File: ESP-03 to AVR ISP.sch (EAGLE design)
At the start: 17 parts, among them J1 AVR_SPI_PRG_62X3_LOCK, Q1 MOSFET-NCHANNELBSS138

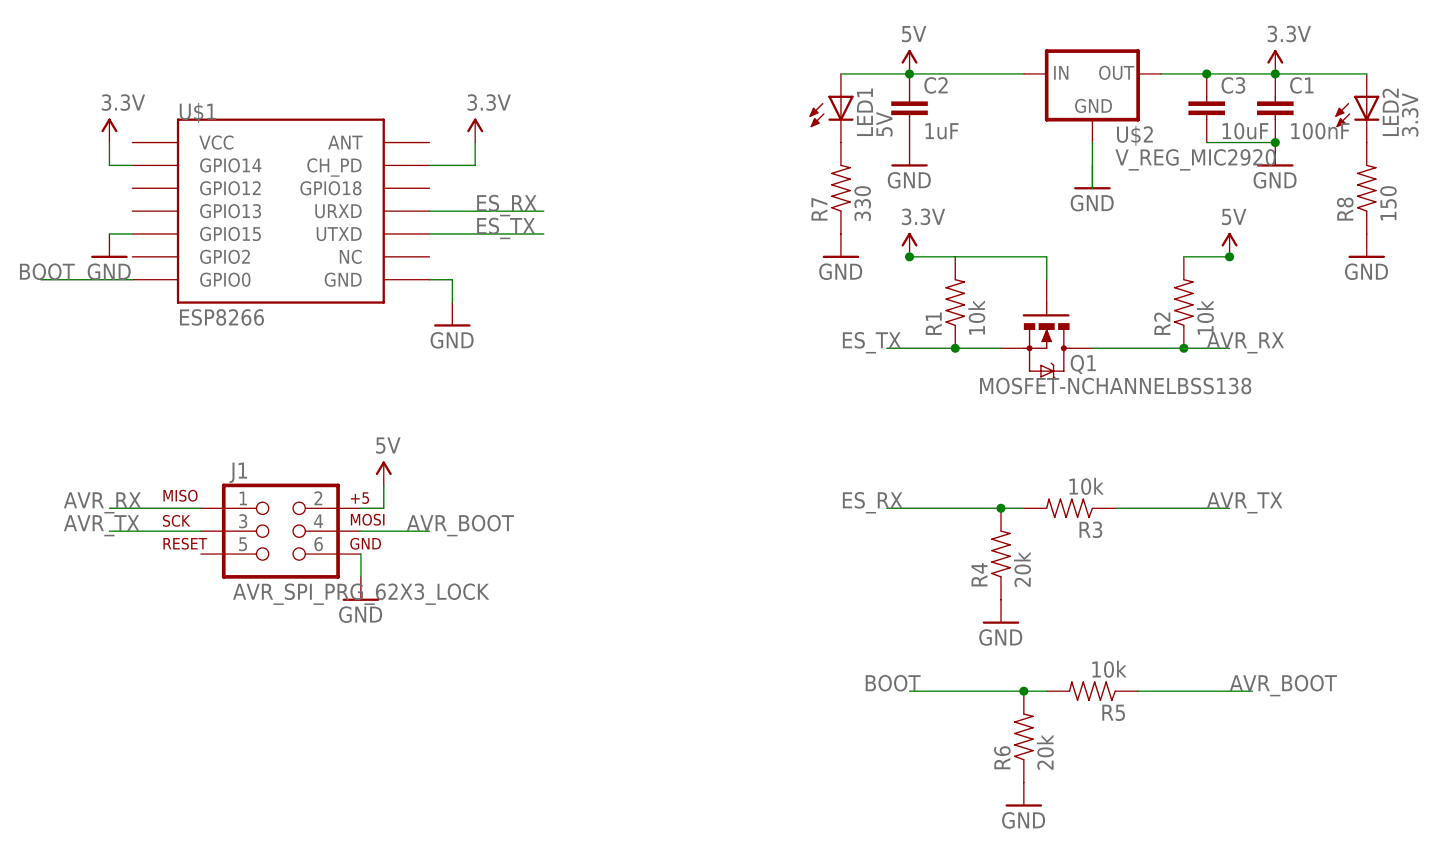
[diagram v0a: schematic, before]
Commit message: PCB: Fixed wrong VCC connection. Removed Bootloader voltage divider. Changed LDO to 1117type
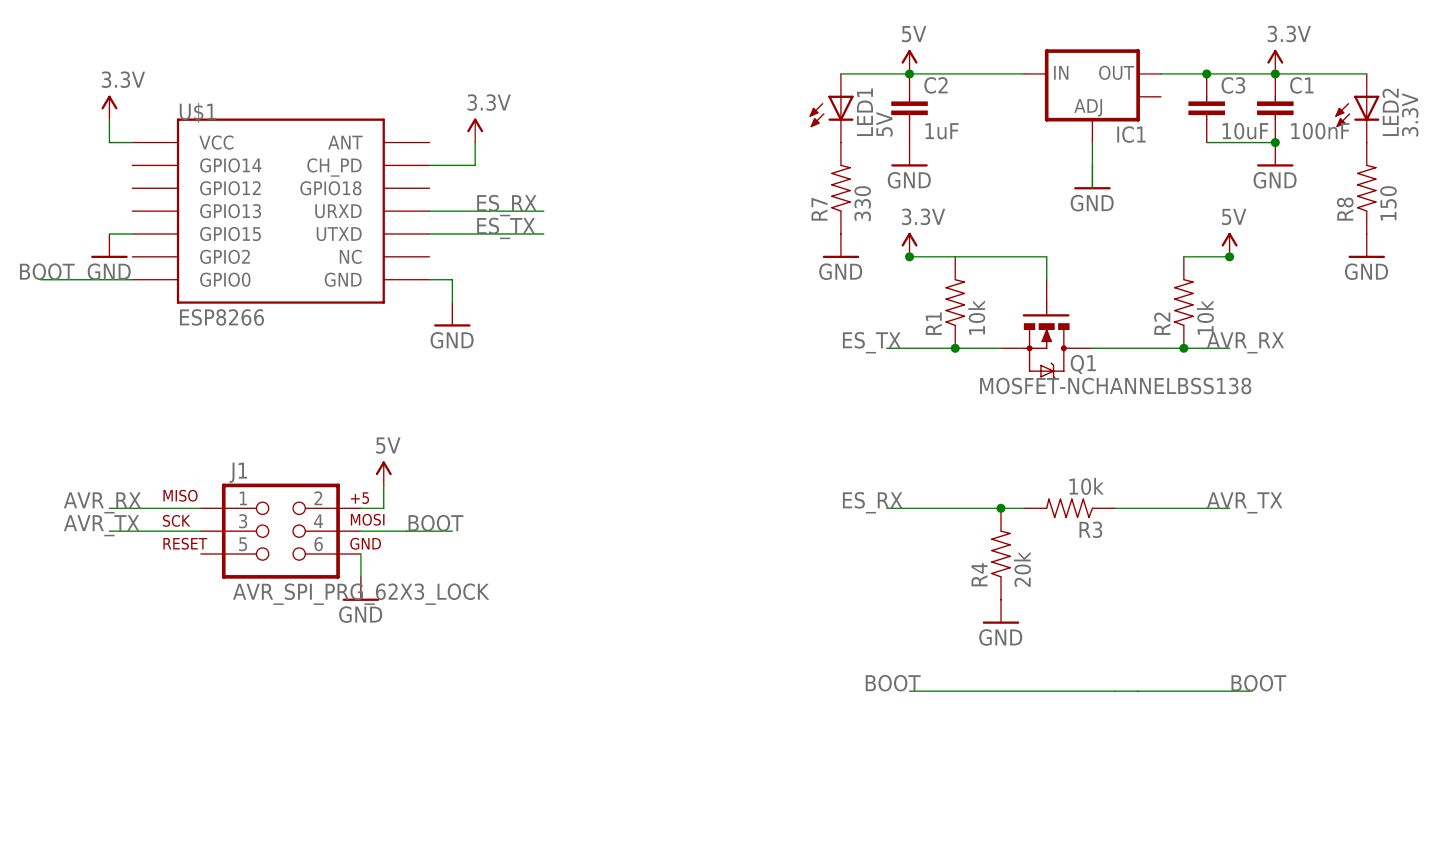
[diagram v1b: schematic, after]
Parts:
- removed R5: 10k, SparkFun-Resistors:RESISTOR0603-RES
- removed R6: 20k, SparkFun-Resistors:RESISTOR0603-RES
- removed U$2: V_REG_MIC2920, SparkFun-PowerIC:V_REG_MIC2920
- added IC1: (no value), SparkFun-PowerIC:V_REG_LM1117SOT223
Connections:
- removed net AVR_BOOT: J1.4, R5.1
- net 3.3V: now also IC1.OUT, U$1.VCC; no longer U$1.GPIO14, U$2.OUT
- net 5V: now also IC1.IN; no longer U$2.IN
- net BOOT: now also J1.4; no longer R5.2, R6.2
- net GND: now also IC1.ADJ; no longer R6.1, U$2.GND
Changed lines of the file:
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@@
 <part name="GND3" library="supply1" deviceset="GND" device=""/>
 <part name="U$1" library="esp8266modules" deviceset="ESP8266" device=""/>
-<part name="U$2" library="SparkFun-PowerIC" deviceset="V_REG_MIC2920" device=""/>
 <part name="J1" library="SparkFun-Connectors" deviceset="AVR_SPI_PRG_6" device="2X3_LOCK"/>
 <part name="SUPPLY1" library="SparkFun-Aesthetics" deviceset="3.3V" device=""/>
@@
 <part name="SUPPLY7" library="SparkFun-Aesthetics" deviceset="5V" device=""/>
 <part name="GND7" library="supply1" deviceset="GND" device=""/>
-<part name="R5" library="SparkFun-Resistors" deviceset="RESISTOR" device="0603-RES" value="10k"/>
-<part name="R6" library="SparkFun-Resistors" deviceset="RESISTOR" device="0603-RES" value="20k"/>
-<part name="GND8" library="supply1" deviceset="GND" device=""/>
 <part name="LED1" library="SparkFun-LED" deviceset="LED" device="0603" value="5V"/>
 <part name="LED2" library="SparkFun-LED" deviceset="LED" device="0603" value="3.3V"/>
@@
 <part name="GND9" library="supply1" deviceset="GND" device=""/>
 <part name="GND10" library="supply1" deviceset="GND" device=""/>
+<part name="IC1" library="SparkFun-PowerIC" deviceset="V_REG_LM1117" device="SOT223"/>
 </parts>
 <sheets>
@@
 <instance part="GND3" gate="1" x="15.24" y="63.5"/>
 <instance part="U$1" gate="G$1" x="-53.34" y="58.42"/>
-<instance part="U$2" gate="G$1" x="35.56" y="73.66"/>
 <instance part="J1" gate="G$1" x="-55.88" y="22.86"/>
 <instance part="SUPPLY1" gate="G$1" x="55.88" y="73.66"/>
@@
 <instance part="GND4" gate="1" x="25.4" y="12.7"/>
 <instance part="SUPPLY3" gate="G$1" x="-33.02" y="66.04"/>
-<instance part="SUPPLY6" gate="G$1" x="-73.66" y="66.04"/>
+<instance part="SUPPLY6" gate="G$1" x="-73.66" y="68.58"/>
 <instance part="GND5" gate="1" x="-35.56" y="45.72"/>
 <instance part="GND6" gate="1" x="-73.66" y="53.34"/>
 <instance part="SUPPLY7" gate="G$1" x="-43.18" y="27.94"/>
 <instance part="GND7" gate="1" x="-45.72" y="15.24"/>
-<instance part="R5" gate="G$1" x="35.56" y="5.08" rot="R180"/>
-<instance part="R6" gate="G$1" x="27.94" y="0" rot="R90"/>
-<instance part="GND8" gate="1" x="27.94" y="-7.62"/>
 <instance part="LED1" gate="G$1" x="7.62" y="71.12"/>
 <instance part="LED2" gate="G$1" x="66.04" y="71.12"/>
@@
 <instance part="GND9" gate="1" x="7.62" y="53.34"/>
 <instance part="GND10" gate="1" x="66.04" y="53.34"/>
+<instance part="IC1" gate="G$1" x="35.56" y="73.66"/>
 </instances>
 <busses>
@@
 <pinref part="GND1" gate="1" pin="GND"/>
 <wire x1="35.56" y1="63.5" x2="35.56" y2="60.96" width="0.1524" layer="91"/>
-<pinref part="U$2" gate="G$1" pin="GND"/>
 <wire x1="35.56" y1="66.04" x2="35.56" y2="63.5" width="0.1524" layer="91"/>
+<pinref part="IC1" gate="G$1" pin="ADJ"/>
 </segment>
 <segment>
@@
 <pinref part="J1" gate="G$1" pin="6"/>
 <wire x1="-45.72" y1="17.78" x2="-45.72" y2="20.32" width="0.1524" layer="91"/>
-</segment>
-<segment>
-<pinref part="R6" gate="G$1" pin="1"/>
-<pinref part="GND8" gate="1" pin="GND"/>
 </segment>
 <segment>
@@
 <wire x1="55.88" y1="73.66" x2="48.26" y2="73.66" width="0.1524" layer="91"/>
 <junction x="55.88" y="73.66"/>
-<pinref part="U$2" gate="G$1" pin="OUT"/>
 <pinref part="SUPPLY1" gate="G$1" pin="3.3V"/>
 <pinref part="C3" gate="G$1" pin="1"/>
@@
 <pinref part="LED2" gate="G$1" pin="A"/>
 <wire x1="55.88" y1="73.66" x2="66.04" y2="73.66" width="0.1524" layer="91"/>
+<pinref part="IC1" gate="G$1" pin="OUT"/>
 </segment>
 <segment>
@@
 </segment>
 <segment>
-<pinref part="U$1" gate="G$1" pin="GPIO14"/>
 <pinref part="SUPPLY6" gate="G$1" pin="3.3V"/>
-<wire x1="-71.12" y1="63.5" x2="-73.66" y2="63.5" width="0.1524" layer="91"/>
-<wire x1="-73.66" y1="63.5" x2="-73.66" y2="66.04" width="0.1524" layer="91"/>
+<wire x1="-73.66" y1="66.04" x2="-73.66" y2="68.58" width="0.1524" layer="91"/>
+<pinref part="U$1" gate="G$1" pin="VCC"/>
+<wire x1="-73.66" y1="66.04" x2="-71.12" y2="66.04" width="0.1524" layer="91"/>
 </segment>
 </net>
@@
 <wire x1="15.24" y1="73.66" x2="27.94" y2="73.66" width="0.1524" layer="91"/>
 <junction x="15.24" y="73.66"/>
-<pinref part="U$2" gate="G$1" pin="IN"/>
 <pinref part="SUPPLY4" gate="G$1" pin="5V"/>
 <pinref part="LED1" gate="G$1" pin="A"/>
 <wire x1="7.62" y1="73.66" x2="15.24" y2="73.66" width="0.1524" layer="91"/>
+<pinref part="IC1" gate="G$1" pin="IN"/>
 </segment>
 <segment>
@@
 </segment>
 <segment>
-<pinref part="R5" gate="G$1" pin="2"/>
-<pinref part="R6" gate="G$1" pin="2"/>
-<wire x1="30.48" y1="5.08" x2="27.94" y2="5.08" width="0.1524" layer="91"/>
-<wire x1="27.94" y1="5.08" x2="15.24" y2="5.08" width="0.1524" layer="91"/>
+<wire x1="53.34" y1="5.08" x2="40.64" y2="5.08" width="0.1524" layer="91"/>
 <label x="10.16" y="5.08" size="1.778" layer="95"/>
-<junction x="27.94" y="5.08"/>
-</segment>
-</net>
-<net name="AVR_BOOT" class="0">
-<segment>
-<pinref part="R5" gate="G$1" pin="1"/>
-<wire x1="40.64" y1="5.08" x2="53.34" y2="5.08" width="0.1524" layer="91"/>
 <label x="50.8" y="5.08" size="1.778" layer="95"/>
+<wire x1="38.1" y1="5.08" x2="15.24" y2="5.08" width="0.1524" layer="91"/>
+<wire x1="40.64" y1="5.08" x2="38.1" y2="5.08" width="0.1524" layer="91"/>
 </segment>
 <segment>
 <pinref part="J1" gate="G$1" pin="4"/>
-<wire x1="-45.72" y1="22.86" x2="-38.1" y2="22.86" width="0.1524" layer="91"/>
+<wire x1="-45.72" y1="22.86" x2="-40.64" y2="22.86" width="0.1524" layer="91"/>
 <label x="-40.64" y="22.86" size="1.778" layer="95"/>
-</segment>
-</net>
+<wire x1="-40.64" y1="22.86" x2="-38.1" y2="22.86" width="0.1524" layer="91"/>
+<wire x1="-35.56" y1="22.86" x2="-38.1" y2="22.86" width="0.1524" layer="91"/>
+</segment>
+</net>

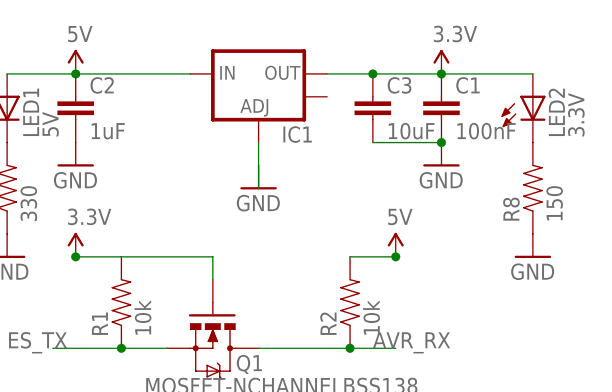
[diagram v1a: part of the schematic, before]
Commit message: Fixed PCB. Swithed to 1117 LDO.
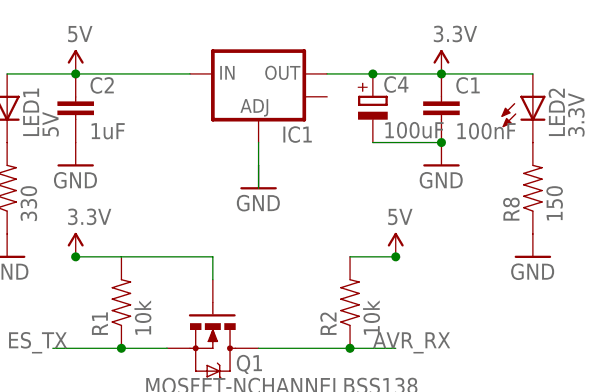
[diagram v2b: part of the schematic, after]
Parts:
- removed C3: 10uF, SparkFun-Capacitors:CAP0603-CAP
- added C4: 100uF, rcl:CPOL-EUB/3528-21R
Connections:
- net 3.3V: now also C4.+; no longer C3.1
- net GND: now also C4.-; no longer C3.2
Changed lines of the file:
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@@
 <part name="SUPPLY4" library="SparkFun-Aesthetics" deviceset="5V" device=""/>
 <part name="SUPPLY5" library="SparkFun-Aesthetics" deviceset="5V" device=""/>
-<part name="C3" library="SparkFun-Capacitors" deviceset="CAP" device="0603-CAP" value="10uF"/>
 <part name="R3" library="SparkFun-Resistors" deviceset="RESISTOR" device="0603-RES" value="10k"/>
 <part name="R4" library="SparkFun-Resistors" deviceset="RESISTOR" device="0603-RES" value="20k"/>
@@
 <part name="GND10" library="supply1" deviceset="GND" device=""/>
 <part name="IC1" library="SparkFun-PowerIC" deviceset="V_REG_LM1117" device="SOT223"/>
+<part name="C4" library="rcl" deviceset="CPOL-EU" device="B/3528-21R" value="100uF"/>
 </parts>
 <sheets>
@@
 <instance part="SUPPLY4" gate="G$1" x="15.24" y="73.66"/>
 <instance part="SUPPLY5" gate="G$1" x="50.8" y="53.34"/>
-<instance part="C3" gate="G$1" x="48.26" y="68.58"/>
 <instance part="R3" gate="G$1" x="33.02" y="25.4" rot="R180"/>
 <instance part="R4" gate="G$1" x="25.4" y="20.32" rot="R90"/>
@@
 <instance part="GND10" gate="1" x="66.04" y="53.34"/>
 <instance part="IC1" gate="G$1" x="35.56" y="73.66"/>
+<instance part="C4" gate="G$1" x="48.26" y="71.12"/>
 </instances>
 <busses>
@@
 <pinref part="C1" gate="G$1" pin="2"/>
 <pinref part="GND2" gate="1" pin="GND"/>
-<pinref part="C3" gate="G$1" pin="2"/>
 <wire x1="48.26" y1="66.04" x2="55.88" y2="66.04" width="0.1524" layer="91"/>
 <junction x="55.88" y="66.04"/>
+<pinref part="C4" gate="G$1" pin="-"/>
 </segment>
 <segment>
@@
 <junction x="55.88" y="73.66"/>
 <pinref part="SUPPLY1" gate="G$1" pin="3.3V"/>
-<pinref part="C3" gate="G$1" pin="1"/>
+<pinref part="LED2" gate="G$1" pin="A"/>
 <wire x1="48.26" y1="73.66" x2="43.18" y2="73.66" width="0.1524" layer="91"/>
-<junction x="48.26" y="73.66"/>
-<pinref part="LED2" gate="G$1" pin="A"/>
 <wire x1="55.88" y1="73.66" x2="66.04" y2="73.66" width="0.1524" layer="91"/>
 <pinref part="IC1" gate="G$1" pin="OUT"/>
+<pinref part="C4" gate="G$1" pin="+"/>
+<junction x="48.26" y="73.66"/>
 </segment>
 <segment>
